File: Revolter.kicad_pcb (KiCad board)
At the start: 4 copper layers, 50 x 50 mm, 112 parts, among them IC1 LM5017, IC2 AP65111, IC3 IRSM005, IC4 IRSM005, IC5 IRSM005, J2 TEMP, J3 USB_B_Mini, J4 Conn_01x03_Male, P3 IN+, P4 IN-, P5 MOTOR3, P6 MOTOR2, P7 MOTOR1, Q1 Q_NMOS_GSD, Q2 Q_NMOS_GSD, Q3 Q_NMOS_GSD, U1 STM32F405RGTx, U2 ACS730xLCTR-50AB, U3 ACS730xLCTR-50AB, U4 ACS730xLCTR-50AB, Y1 8MHz

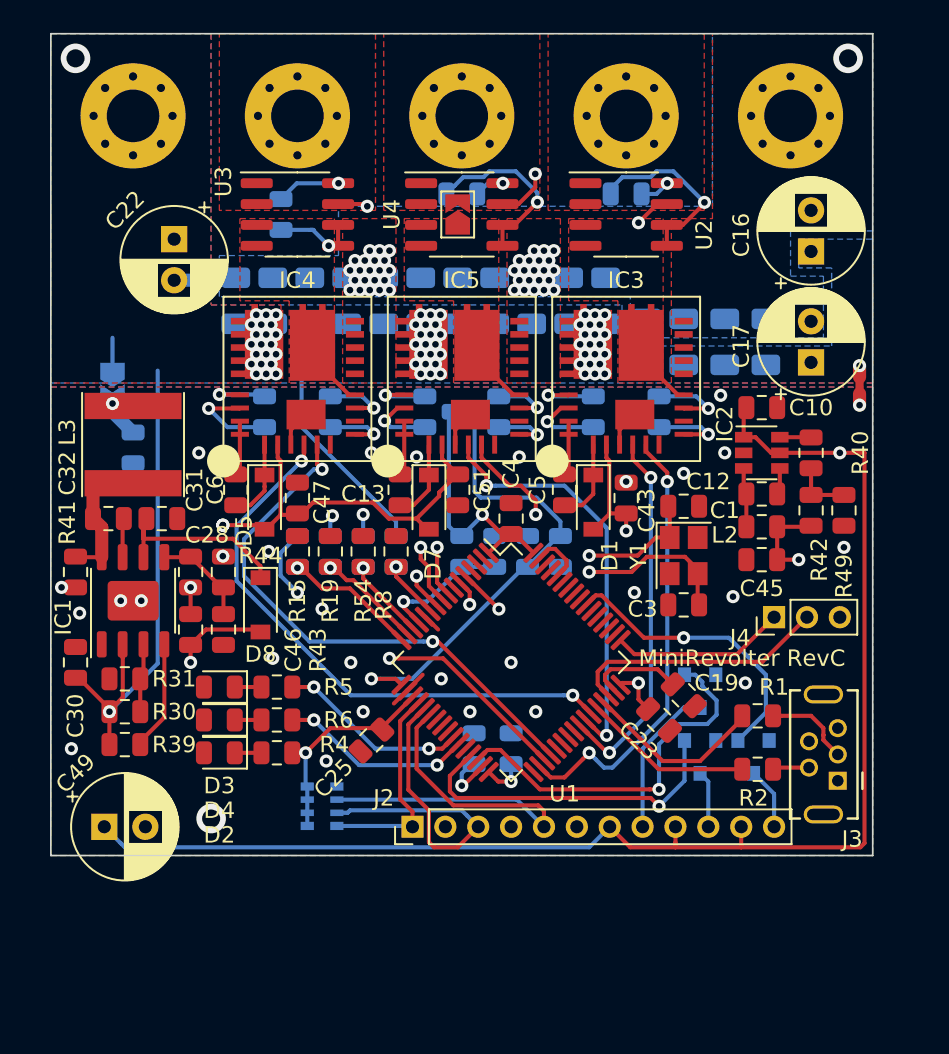
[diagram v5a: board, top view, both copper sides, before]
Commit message: - added flyback diodes to FAN outputs - added fourth DC cap - changed TEMP3 to motor temp
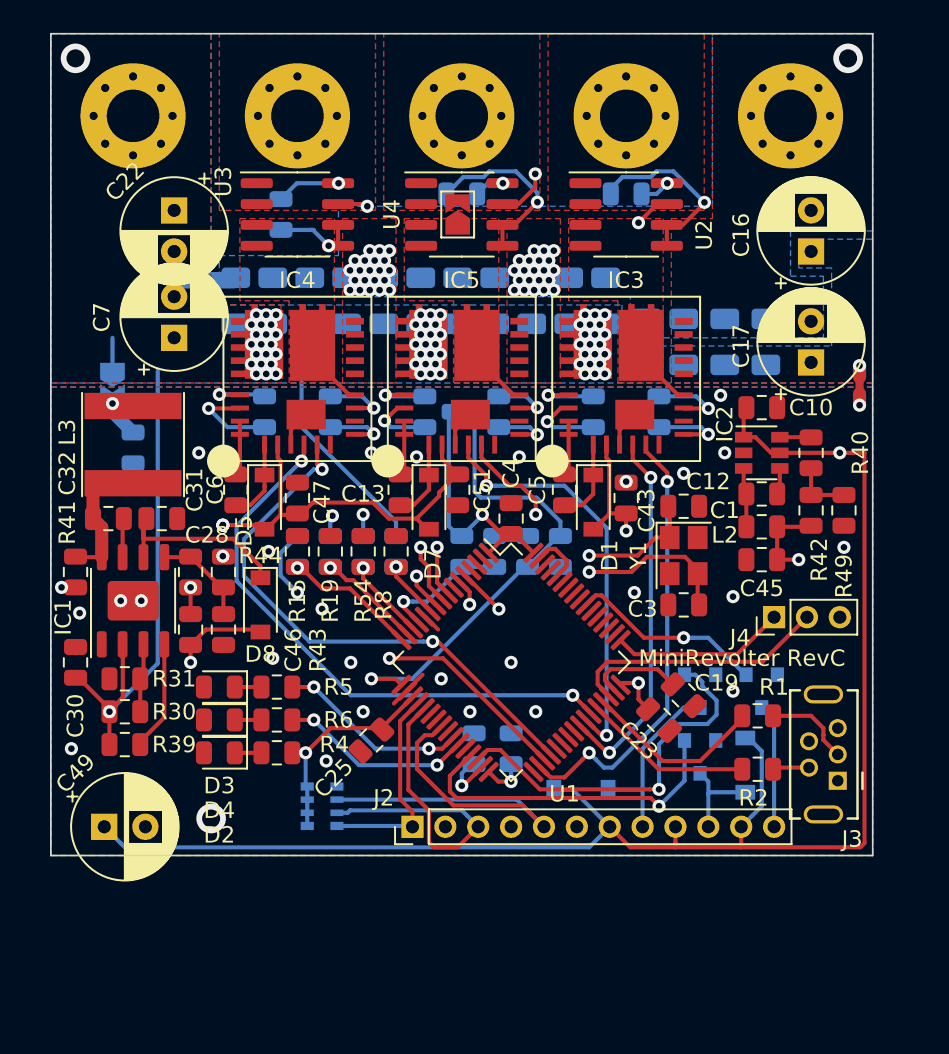
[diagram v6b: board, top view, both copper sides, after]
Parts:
- added C7: CP, Capacitor_THT:CP_Radial_D6.3mm_P2.50mm, F.Cu at (142.5, 43.5)
- added D6: D, Diode_SMD:D_SOD-123, B.Cu at (177.2, 69.5)
- added D9: D, Diode_SMD:D_SOD-123, B.Cu at (167.2, 71.0)
- D8: value 4148 -> D
- U2, U3, U4: value ACS730xLCTR-50AB -> ACS722LLCTR-40AU-T
- moved Q1 4.03 mm to (178.2, 65.0)
- moved C22 1.75 mm to (142.5, 35.8)
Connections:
- J2 pad 5: /TEMP3 -> /TEMP_M
- RN2 pad 2: /TEMP3 -> /TEMP_M
- U1 pad 22: /TEMP3 -> (no net)
- U1 pad 24: (no net) -> /TEMP_M
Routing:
- net /TEMP3: track 26.7 -> 0.00 mm
- net /TEMP_M: track 0.00 -> 26.0 mm
- net +12V: track 170.9 -> 181.6 mm
- net /MCU/PWM_PUMP: track 17.9 -> 12.0 mm
- net /PUMP: track 3.77 -> 7.56 mm
- net GNDPWR: track 4.51 -> 7.26 mm
- net /FAN1: track 3.46 -> 5.75 mm
- net /FAN2: track 9.29 -> 11.4 mm

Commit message: -finishing touches for RevC
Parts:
- moved C48 3.75 mm to (136.2, 50.2)
- moved JP1 2.50 mm to (136.2, 46.2)
- moved C7 1.50 mm to (142.5, 45.0)
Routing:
- net +12V: track 181.6 -> 186.1 mm
- net GNDPWR: track 7.26 -> 8.76 mm
- net +BATT: track 45.7 -> 44.9 mm
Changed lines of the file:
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@@
     (thickness 1.6)
     (drawings 7)
-    (tracks 820)
+    (tracks 824)
     (zones 0)
     (modules 115)
@@
     (34 B.Paste user hide)
     (35 F.Paste user hide)
-    (36 B.SilkS user hide)
-    (37 F.SilkS user hide)
+    (36 B.SilkS user)
+    (37 F.SilkS user)
     (38 B.Mask user hide)
     (39 F.Mask user hide)
@@
   )
   (setup
-    (last_trace_width 0.25)
+    (last_trace_width 1)
     (user_trace_width 0.8)
     (user_trace_width 1)
@@
     (add_net /MCU/PWM_FAN2)
     (add_net /MCU/PWM_PUMP)
-    (add_net /MCU/TEMP_3)
     (add_net /MCU/TEMP_MOSFET)
     (add_net /MCU/USB_DM)
@@
     (tags SOD-123)
     (attr smd)
-    (fp_text reference D9 (at 0 2) (layer B.SilkS)
+    (fp_text reference D9 (at -1 -1.75) (layer B.SilkS)
       (effects (font (size 1 1) (thickness 0.15)) (justify mirror))
     )
@@
     (tags SOD-123)
     (attr smd)
-    (fp_text reference D6 (at 0 2 90) (layer B.SilkS)
+    (fp_text reference D6 (at 0 -2 90) (layer B.SilkS)
       (effects (font (size 1 1) (thickness 0.15)) (justify mirror))
     )
@@
   )
   (module Capacitor_THT:CP_Radial_D6.3mm_P2.50mm (layer F.Cu)
-    (at 142.5 43.5 90)
+    (at 142.5 45 90)
     (descr "CP, Radial series, Radial, pin pitch=2.50mm, , diameter=6.3mm, Electrolytic Capacitor")
     (tags "CP Radial series Radial pin pitch 2.50mm  diameter 6.3mm Electrolytic Capacitor")
@@
     (descr "CP, Radial series, Radial, pin pitch=2.50mm, , diameter=6.3mm, Electrolytic Capacitor")
     (tags "CP Radial series Radial pin pitch 2.50mm  diameter 6.3mm Electrolytic Capacitor")
-    (fp_text reference C22 (at -1.75 3 225) (layer F.SilkS)
+    (fp_text reference C22 (at 1.25 4.5 270) (layer F.SilkS)
       (effects (font (size 1 1) (thickness 0.15)))
     )
@@
     (tags SOT-23)
     (attr smd)
-    (fp_text reference Q1 (at 2.5 0) (layer B.SilkS)
+    (fp_text reference Q1 (at -2.5 0) (layer B.SilkS)
       (effects (font (size 1 1) (thickness 0.15)) (justify mirror))
     )
@@
   )
   (module Jumper:SolderJumper-2_P1.3mm_Open_TrianglePad1.0x1.5mm (layer B.Cu)
-    (at 138.75 46.25 270)
+    (at 136.25 46.25 270)
     (descr "SMD Solder Jumper, 1x1.5mm Triangular Pads, 0.3mm gap, open")
     (tags "solder jumper open")
@@
   )
   (module Capacitor_SMD:C_0805_2012Metric (layer B.Cu)
-    (at 140 50.2 270)
+    (at 136.25 50.25 270)
     (descr "Capacitor SMD 0805 (2012 Metric), square (rectangular) end terminal, IPC_7351 nominal, (Body size source: https://docs.google.com/spreadsheets/d/1BsfQQcO9C6DZCsRaXUlFlo91Tg2WpOkGARC1WS5S8t0/edit?usp=sharing), generated with kicad-footprint-generator")
     (tags capacitor)
@@
   (segment (start 184.2 45.2) (end 184.2 45.2) (width 0.8) (layer F.Cu) (net 1))
   (via (at 184.2 45.2) (size 0.8) (drill 0.4) (layers F.Cu B.Cu) (net 1))
-  (segment (start 142.5 38.25) (end 142.5 41) (width 1) (layer B.Cu) (net 1))
+  (segment (start 142.5 38.25) (end 142.5 42.5) (width 1) (layer B.Cu) (net 1))
   (via (at 172.5 34.1) (size 0.8) (drill 0.4) (layers F.Cu B.Cu) (net 2))
   (via (at 162.5 34.1) (size 0.8) (drill 0.4) (layers F.Cu B.Cu) (net 2))
@@
   (segment (start 138.5625 66.25) (end 138.5625 68.25) (width 0.25) (layer F.Cu) (net 3))
   (via (at 138.5625 66.25) (size 0.8) (drill 0.4) (layers F.Cu B.Cu) (net 3))
-  (segment (start 138.75 45.525) (end 138.75 43.5) (width 0.25) (layer B.Cu) (net 3))
   (segment (start 138.5625 66.25) (end 141.5 63.3125) (width 0.25) (layer B.Cu) (net 3))
   (segment (start 141.5 63.3125) (end 141.5 45.5) (width 0.25) (layer B.Cu) (net 3))
@@
   (segment (start 156 55.5625) (end 156 54.676998) (width 0.25) (layer B.Cu) (net 3))
   (segment (start 156 54.676998) (end 150.25 48.926998) (width 0.25) (layer B.Cu) (net 3))
+  (segment (start 136.25 45.525) (end 136.25 44.25) (width 0.25) (layer B.Cu) (net 3))
   (segment (start 140.4375 68.25) (end 140.4375 68.0625) (width 0.25) (layer F.Cu) (net 4))
   (segment (start 141.905 66.595) (end 141.905 62.15) (width 0.25) (layer F.Cu) (net 4))
@@
   (segment (start 178.815 50.5) (end 179.35 50.5) (width 0.25) (layer F.Cu) (net 18))
   (segment (start 177.865 49.55) (end 178.815 50.5) (width 0.25) (layer F.Cu) (net 18))
-  (segment (start 138.75 48.0125) (end 140 49.2625) (width 0.8) (layer B.Cu) (net 18))
-  (segment (start 138.75 47.5) (end 138.75 48.0125) (width 0.8) (layer B.Cu) (net 18))
-  (via (at 138.75 47.5) (size 0.8) (drill 0.4) (layers F.Cu B.Cu) (net 18))
   (via (at 143.5 63.25) (size 0.8) (drill 0.4) (layers F.Cu B.Cu) (net 18))
   (segment (start 143.5 63.25) (end 143.5 62.1875) (width 0.25) (layer F.Cu) (net 18))
@@
   (segment (start 138.25 68.5) (end 138.25 73.25) (width 0.25) (layer Sig) (net 18))
   (segment (start 143.5 63.25) (end 138.25 68.5) (width 0.25) (layer Sig) (net 18))
-  (segment (start 138.75 47.5) (end 138.75 46.975) (width 0.25) (layer B.Cu) (net 18))
   (segment (start 147.75 54.9) (end 148 55.15) (width 0.25) (layer F.Cu) (net 18))
   (segment (start 145.4625 54.9) (end 145.4625 54.9) (width 0.25) (layer F.Cu) (net 18))
@@
   (segment (start 145.4625 54.9) (end 147.75 54.9) (width 0.25) (layer F.Cu) (net 18))
   (via (at 145.4625 54.9) (size 0.8) (drill 0.4) (layers F.Cu B.Cu) (net 18))
-  (segment (start 138.75 48.1875) (end 138.75 47.5) (width 0.25) (layer Sig) (net 18))
-  (segment (start 145.4625 54.9) (end 138.75 48.1875) (width 0.25) (layer Sig) (net 18))
   (segment (start 145.4625 61.2875) (end 143.5 63.25) (width 0.25) (layer Sig) (net 18))
   (segment (start 145.4625 54.9) (end 145.4625 56.7875) (width 0.25) (layer Sig) (net 18))
@@
   (via (at 170 55.25) (size 0.8) (drill 0.4) (layers F.Cu B.Cu) (net 18))
   (segment (start 170 54.1875) (end 170 55.25) (width 0.25) (layer F.Cu) (net 18))
-  (segment (start 184.5 74.25) (end 184.5 50.5) (width 0.25) (layer F.Cu) (net 18))
-  (segment (start 184.5 50.5) (end 179.35 50.5) (width 0.25) (layer F.Cu) (net 18))
-  (segment (start 177 74.5) (end 184.25 74.5) (width 0.25) (layer F.Cu) (net 18))
-  (segment (start 184.25 74.5) (end 184.5 74.25) (width 0.25) (layer F.Cu) (net 18))
   (via (at 183 50.5) (size 0.8) (drill 0.4) (layers F.Cu B.Cu) (net 18))
   (segment (start 178.25 55.25) (end 183 50.5) (width 0.25) (layer Sig) (net 18))
@@
   (segment (start 166.75 71) (end 169 73.25) (width 0.25) (layer B.Cu) (net 18))
   (segment (start 165.6 71) (end 166.75 71) (width 0.25) (layer B.Cu) (net 18))
+  (segment (start 145.4625 54.9) (end 142.9 54.9) (width 0.25) (layer Sig) (net 18))
+  (via (at 136.25 48.25) (size 0.8) (drill 0.4) (layers F.Cu B.Cu) (net 18))
+  (segment (start 136.649999 48.649999) (end 136.25 48.25) (width 0.25) (layer Sig) (net 18))
+  (segment (start 142.9 54.9) (end 136.649999 48.649999) (width 0.25) (layer Sig) (net 18))
+  (segment (start 136.25 48.25) (end 136.75 47.75) (width 1) (layer F.Cu) (net 18))
+  (segment (start 139.9 47.75) (end 140 47.65) (width 1) (layer F.Cu) (net 18))
+  (segment (start 136.75 47.75) (end 139.9 47.75) (width 1) (layer F.Cu) (net 18))
+  (segment (start 136.25 49.3125) (end 136.25 48.25) (width 1) (layer B.Cu) (net 18))
+  (segment (start 136.25 48.25) (end 136.25 46.975) (width 0.25) (layer B.Cu) (net 18))
+  (segment (start 183 50.5) (end 179.35 50.5) (width 0.25) (layer F.Cu) (net 18))
+  (segment (start 184.5 52) (end 183 50.5) (width 0.25) (layer F.Cu) (net 18))
+  (segment (start 177 74.5) (end 184.25 74.5) (width 0.25) (layer F.Cu) (net 18))
+  (segment (start 184.5 74.25) (end 184.5 52) (width 0.25) (layer F.Cu) (net 18))
+  (segment (start 184.25 74.5) (end 184.5 74.25) (width 0.25) (layer F.Cu) (net 18))
   (segment (start 145.5 58.6875) (end 145.5 60.3125) (width 0.25) (layer F.Cu) (net 19))
   (segment (start 145.375 58.6875) (end 145.5 58.6875) (width 0.25) (layer F.Cu) (net 19))
@@
   (segment (start 157 73.25) (end 157 72.325) (width 0.25) (layer F.Cu) (net 73))
   (segment (start 157 72.325) (end 156.25 71.575) (width 0.25) (layer F.Cu) (net 73))
-  (segment (start 163.35 71.6) (end 165 73.25) (width 0.25) (layer B.Cu) (net 79))
-  (segment (start 152.4 71.6) (end 163.35 71.6) (width 0.25) (layer B.Cu) (net 79))
   (segment (start 160.325001 72.575001) (end 161 73.25) (width 0.25) (layer B.Cu) (net 74))
   (segment (start 159.999999 72.249999) (end 160.325001 72.575001) (width 0.25) (layer B.Cu) (net 74))
@@
   (segment (start 154 57.4375) (end 154 58.139088) (width 0.25) (layer F.Cu) (net 78))
   (via (at 154 57.5) (size 0.8) (drill 0.4) (layers F.Cu B.Cu) (net 78))
+  (segment (start 163.35 71.6) (end 165 73.25) (width 0.25) (layer B.Cu) (net 79))
+  (segment (start 152.4 71.6) (end 163.35 71.6) (width 0.25) (layer B.Cu) (net 79))
   (segment (start 158.215927 67.680519) (end 158.810392 67.086054) (width 0.25) (layer F.Cu) (net 79))
   (segment (start 157.746479 67.680519) (end 158.215927 67.680519) (width 0.25) (layer F.Cu) (net 79))

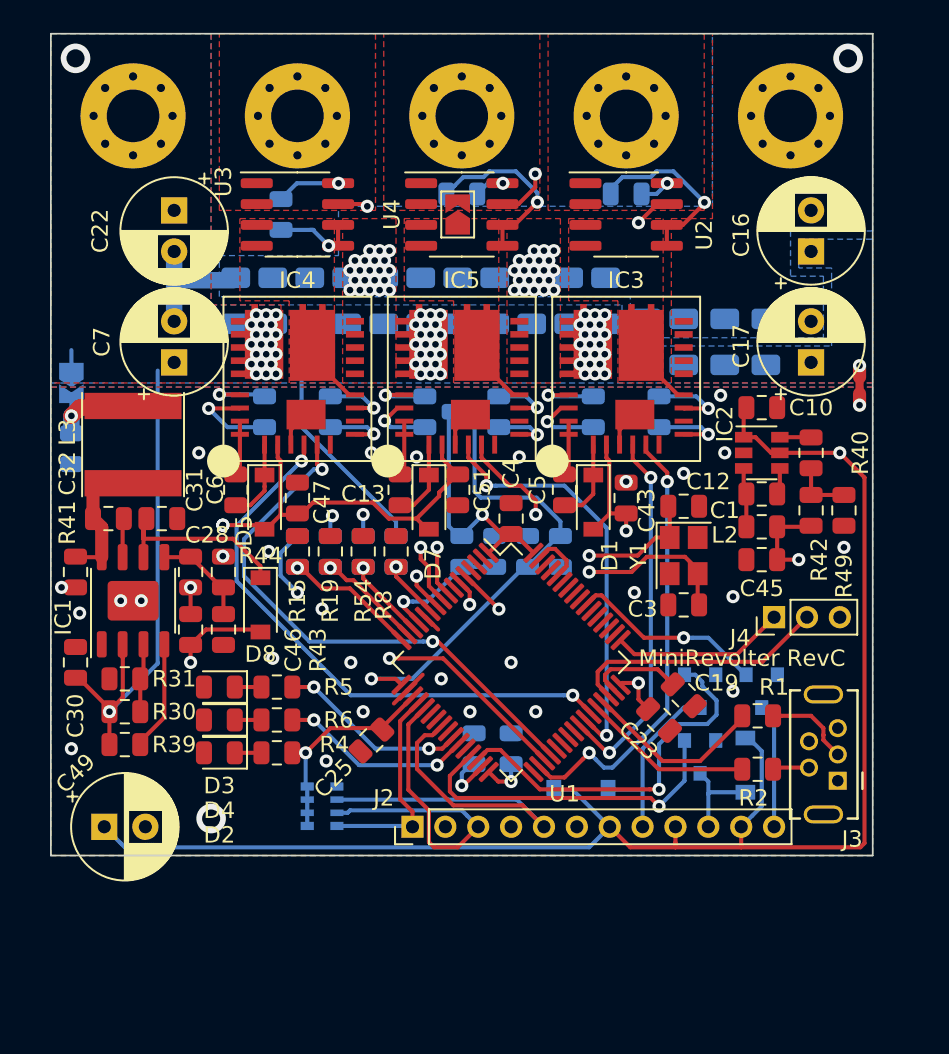
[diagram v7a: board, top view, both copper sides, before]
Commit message: - removed Temp3 input - removed hall input - removed CAN - added HMI UART - added freewheeling diode to pump output - moved temp connector left to mitigate collision with USB - added fourth pinhole for pasting
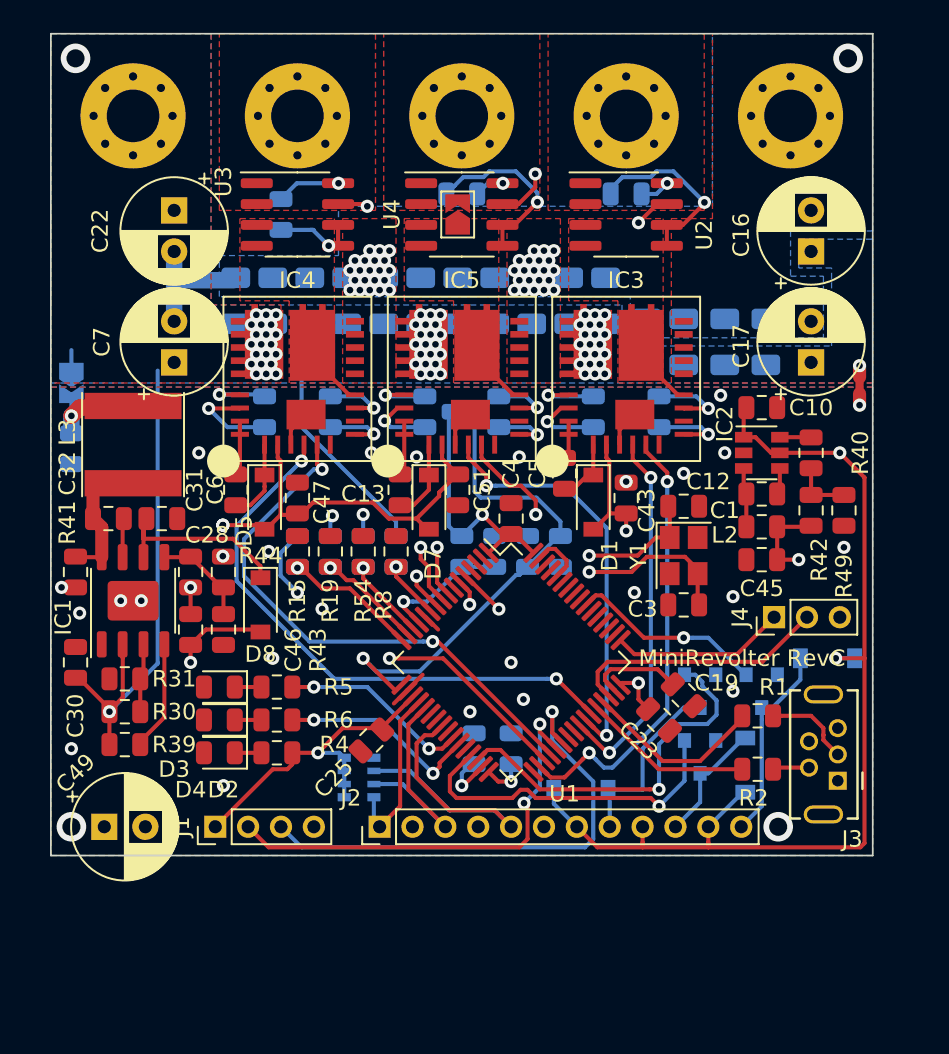
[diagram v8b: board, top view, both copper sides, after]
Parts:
- added D10: D, Diode_SMD:D_SOD-123, B.Cu at (182.2, 63.0)
- added J1: HMI, Connector_PinHeader_2.00mm:PinHeader_1x04_P2.00mm_Vertical, F.Cu at (145.0, 73.2)
- J4: value Conn_01x03_Male -> Conn_01x03
- moved RN2 2.85 mm to (153.8, 70.2)
- moved J2 2.00 mm to (155.0, 73.2)
- moved C5 1.00 mm to (166.2, 51.8)
- turned D6 to 90 degrees
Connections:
- U1 pad 37: (no net) -> /MCU/HMI_TX
- U1 pad 38: (no net) -> /MCU/HMI_RX
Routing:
- net /MCU/HMI_RX: track 0.00 -> 30.7 mm, vias 0 -> 1
- net /MCU/HMI_TX: track 0.00 -> 27.1 mm, vias 0 -> 2
- net /TEMP2: track 21.8 -> 14.0 mm
- net +3V3: track 109.1 -> 115.7 mm
- net /TEMP_M: track 26.0 -> 20.8 mm
- net /PUMP: track 7.56 -> 12.1 mm
- net +12V: track 186.1 -> 183.1 mm, vias 7 -> 8
- net /TEMP1: track 13.0 -> 10.5 mm
- net /MCU/TEMP_MOSFET: track 28.8 -> 30.8 mm
- net /FAN1: track 5.75 -> 7.51 mm
- net Net-(C5-Pad1): track 5.03 -> 3.95 mm
- net Net-(C5-Pad2): track 3.34 -> 2.34 mm
- net /MCU/LED_RED: track 11.9 -> 12.4 mm
- net GND: vias 30 -> 28
